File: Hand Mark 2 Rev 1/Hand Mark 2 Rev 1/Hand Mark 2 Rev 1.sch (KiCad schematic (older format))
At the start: 18 parts, among them J1 Conn_ARM_JTAG_SWD_10, M1 Index_Servo, M2 Middle_Servo, M3 Ring_Servo, M4 Pinky_Servo, M5 Thumb_Servo, SW1 Power_Switch

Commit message: changed 3.3 regulator and added resistor to neopixel data input
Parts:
- removed REG1: ADP7142AUJZ-3.3, Package_TO_SOT_SMD:TSOT-23-5, symbol Regulator_Linear:ADP7142AUJZ-3.3
- added C1, C2: 1uF, symbol Device:C
- added R5: 500ohm, symbol Device:R_US
- added REG1: MIC5504-3.3YM5, Package_TO_SOT_SMD:SOT-23-5, symbol Regulator_Linear:MIC5504-3.3YM5
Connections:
- wire segments 38 -> 42
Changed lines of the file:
@@
 EESchema Schematic File Version 4
+LIBS:Hand Mark 2 Rev 1-cache
 EELAYER 30 0
 EELAYER END
@@
 $EndComp
 $Comp
-L Regulator_Linear:ADP7142AUJZ-3.3 REG1
-U 1 1 5E219EEA
-P 1900 1400
-F 0 "REG1" H 1900 1767 50  0000 C CNN
-F 1 "ADP7142AUJZ-3.3" H 1900 1676 50  0000 C CNN
-F 2 "Package_TO_SOT_SMD:TSOT-23-5" H 1900 1000 50  0001 C CIN
-F 3 "https://www.analog.com/media/en/technical-documentation/data-sheets/ADP7142.pdf" H 1900 900 50  0001 C CNN
-	1    1900 1400
-	1    0    0    -1
-$EndComp
-$Comp
 L power:+3.3V #PWR?
 U 1 1 5E22153D
-P 2550 1300
-F 0 "#PWR?" H 2550 1150 50  0001 C CNN
-F 1 "+3.3V" H 2565 1473 50  0000 C CNN
-F 2 "" H 2550 1300 50  0001 C CNN
-F 3 "" H 2550 1300 50  0001 C CNN
-	1    2550 1300
+P 2250 1200
+F 0 "#PWR?" H 2250 1050 50  0001 C CNN
+F 1 "+3.3V" H 2265 1373 50  0000 C CNN
+F 2 "" H 2250 1200 50  0001 C CNN
+F 3 "" H 2250 1200 50  0001 C CNN
+	1    2250 1200
 	1    0    0    -1
 $EndComp
@@
 	1    0    0    -1
 $EndComp
-Wire Wire Line
-	2300 1300 2550 1300
 $Comp
 L power:+3.3V #PWR?
@@
 L power:GND #PWR?
 U 1 1 5E23530E
-P 1900 1700
-F 0 "#PWR?" H 1900 1450 50  0001 C CNN
-F 1 "GND" H 1905 1527 50  0000 C CNN
-F 2 "" H 1900 1700 50  0001 C CNN
-F 3 "" H 1900 1700 50  0001 C CNN
-	1    1900 1700
+P 1700 1800
+F 0 "#PWR?" H 1700 1550 50  0001 C CNN
+F 1 "GND" H 1705 1627 50  0000 C CNN
+F 2 "" H 1700 1800 50  0001 C CNN
+F 3 "" H 1700 1800 50  0001 C CNN
+	1    1700 1800
 	1    0    0    -1
 $EndComp
@@
 L power:+BATT #PWR?
 U 1 1 5E249F42
-P 1300 1300
-F 0 "#PWR?" H 1300 1150 50  0001 C CNN
-F 1 "+BATT" H 1315 1473 50  0000 C CNN
-F 2 "" H 1300 1300 50  0001 C CNN
-F 3 "" H 1300 1300 50  0001 C CNN
-	1    1300 1300
-	1    0    0    -1
-$EndComp
-Wire Wire Line
-	1500 1300 1300 1300
+P 1150 1200
+F 0 "#PWR?" H 1150 1050 50  0001 C CNN
+F 1 "+BATT" H 1165 1373 50  0000 C CNN
+F 2 "" H 1150 1200 50  0001 C CNN
+F 3 "" H 1150 1200 50  0001 C CNN
+	1    1150 1200
+	1    0    0    -1
+$EndComp
 Text GLabel 7600 1350 2    50   Input ~ 0
 MYOSIG
@@
 Wire Wire Line
 	5600 3400 5700 3400
-Text GLabel 7300 4500 0    50   Input ~ 0
+Text GLabel 7100 4500 0    50   Input ~ 0
 NEO
-Wire Wire Line
-	7300 4500 7400 4500
 $Comp
 L power:+5V #PWR?
@@
 	1    0    0    -1
 $EndComp
+$Comp
+L Regulator_Linear:MIC5504-3.3YM5 REG1
+U 1 1 5E20BBC0
+P 1700 1300
+F 0 "REG1" H 1700 1667 50  0000 C CNN
+F 1 "MIC5504-3.3YM5" H 1700 1576 50  0000 C CNN
+F 2 "Package_TO_SOT_SMD:SOT-23-5" H 1700 900 50  0001 C CNN
+F 3 "http://ww1.microchip.com/downloads/en/DeviceDoc/MIC550X.pdf" H 1450 1550 50  0001 C CNN
+	1    1700 1300
+	1    0    0    -1
+$EndComp
+Wire Wire Line
+	2100 1200 2250 1200
+Wire Wire Line
+	1150 1200 1300 1200
+$Comp
+L Device:C C2
+U 1 1 5E21B87C
+P 2250 1650
+F 0 "C2" H 2365 1696 50  0000 L CNN
+F 1 "1uF" H 2365 1605 50  0000 L CNN
+F 2 "" H 2288 1500 50  0001 C CNN
+F 3 "~" H 2250 1650 50  0001 C CNN
+	1    2250 1650
+	1    0    0    -1
+$EndComp
+$Comp
+L Device:C C1
+U 1 1 5E21CD0A
+P 1150 1650
+F 0 "C1" H 1265 1696 50  0000 L CNN
+F 1 "1uF" H 1265 1605 50  0000 L CNN
+F 2 "" H 1188 1500 50  0001 C CNN
+F 3 "~" H 1150 1650 50  0001 C CNN
+	1    1150 1650
+	1    0    0    -1
+$EndComp
+Wire Wire Line
+	2250 1200 2250 1500
+Connection ~ 2250 1200
+Wire Wire Line
+	1150 1200 1150 1500
+Connection ~ 1150 1200
+Wire Wire Line
+	1700 1600 1700 1800
+Wire Wire Line
+	1150 1800 1700 1800
+Connection ~ 1700 1800
+Wire Wire Line
+	1700 1800 2250 1800
+$Comp
+L Device:R_US R5
+U 1 1 5E2292AF
+P 7250 4500
+F 0 "R5" V 7045 4500 50  0000 C CNN
+F 1 "500ohm" V 7136 4500 50  0000 C CNN
+F 2 "" V 7290 4490 50  0001 C CNN
+F 3 "~" H 7250 4500 50  0001 C CNN
+	1    7250 4500
+	0    1    1    0
+$EndComp
 $EndSCHEMATC

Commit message: charger and 5v regulator added. should be ready for breadboard prototyping.
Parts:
- added C? (x2): 4.7uF, symbol Device:C
- added C?: 4.7uF 10V, symbol Device:C
- added C?: 22uF 10V, symbol Device:C
- added L?: 1uH 3A, symbol Device:L
- added LED?: Charging_LED, symbol Device:LED
- added LED?: Charge_Done_LED, symbol Device:LED
- added R?: 2000ohm, symbol Device:R_US
- added R? (x2): 470ohm, symbol Device:R_US
- added R?: 1Mohm, symbol Device:R_US
- added REG?: MIC2876-5.5YMT-TR, symbol hand~parts:MIC2876-5.5YMT-TR
- added USB?: USB_B_Micro, symbol Connector:USB_B_Micro
- renumbered BT1 to BT?, BTN1 to BTN?, C2 to C?, C1 to C?, CHRG1 to CHRG?, J1 to J?, M1 to M?, M2 to M?, M3 to M?, M4 to M?, M5 to M?, MCU1 to MCU?, MYO1 to MYO?, D1 to NEO?, R5 to R?, R1 to R?, R2 to R?, R3 to R?, R4 to R?, REG1 to REG?, SW1 to SW?
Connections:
- wire segments 42 -> 75
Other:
- moved on the sheet: BT?, BTN?, C?, CHRG?, J?, MCU?, NEO?, R?, REG?, SW?

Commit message: starting pcb layout done
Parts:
- BT1: renamed from BT?; footprint (none) -> Connector_JST:JST_EH_S2B-EH_1x02_P2.50mm_Horizontal
- BTN1: renamed from BTN?; footprint (none) -> Connector_JST:JST_EH_S2B-EH_1x02_P2.50mm_Horizontal
- C1, C2, C3, C4, C5, C6: renamed from C?; footprint (none) -> Capacitor_SMD:C_0805_2012Metric_Pad1.15x1.40mm_HandSolder
- J1: renamed from J?; footprint (none) -> Connector_PinHeader_1.27mm:PinHeader_2x05_P1.27mm_Vertical
- L1: renamed from L?; footprint (none) -> Inductor_SMD:L_1210_3225Metric_Pad1.42x2.65mm_HandSolder
- LED1, LED2: renamed from LED?; footprint (none) -> Connector_JST:JST_EH_S2B-EH_1x02_P2.50mm_Horizontal
- M1, M2, M3, M4, M5: renamed from M?; footprint (none) -> Connector_JST:JST_EH_S3B-EH_1x03_P2.50mm_Horizontal
- MYO1: renamed from MYO?; footprint (none) -> Connector_JST:JST_EH_S3B-EH_1x03_P2.50mm_Horizontal
- NEO1: renamed from NEO?; footprint (none) -> Connector_JST:JST_EH_S3B-EH_1x03_P2.50mm_Horizontal
- R1, R2, R3, R4, R5, R6, R7, R8, R9: renamed from R?; footprint (none) -> Resistor_SMD:R_0805_2012Metric_Pad1.15x1.40mm_HandSolder
- REG2: renamed from REG?; footprint (none) -> Package_DFN_QFN:DFN-8-1EP_2x2mm_P0.5mm_EP0.9x1.3mm
- SW1: renamed from SW?; footprint (none) -> Connector_JST:JST_EH_S2B-EH_1x02_P2.50mm_Horizontal
- USB1: renamed from USB?; footprint (none) -> Connector_JST:JST_EH_S2B-EH_1x02_P2.50mm_Horizontal
- gave numbers to parts that had none: 3

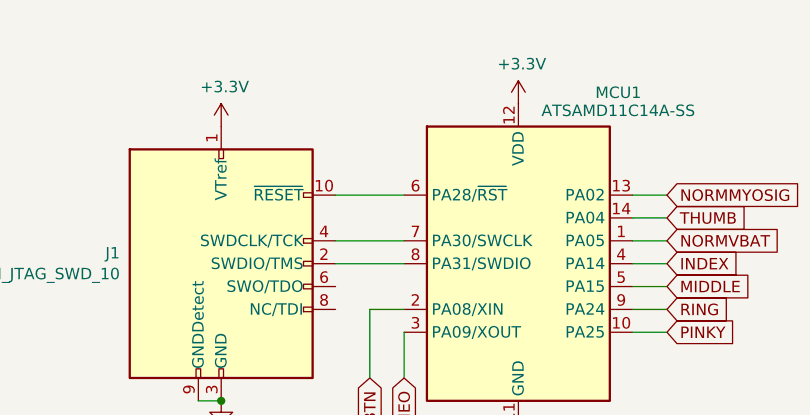
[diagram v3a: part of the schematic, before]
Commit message: finsihed first test routing(need thicker traces for power)
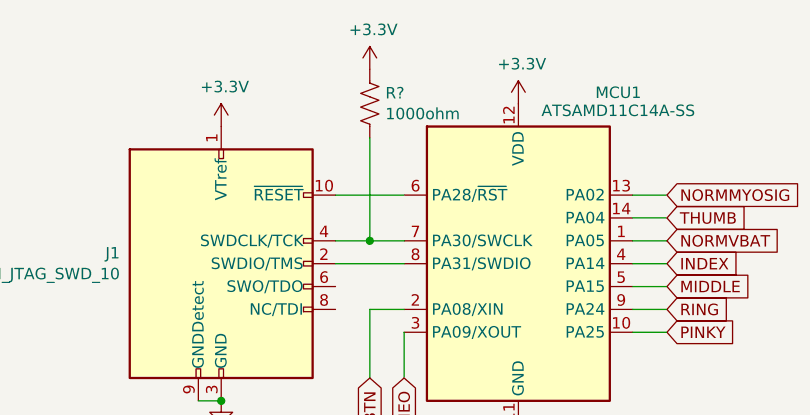
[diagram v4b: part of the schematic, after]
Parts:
- added R?: 1000ohm, symbol Device:R_US
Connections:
- wire segments 75 -> 77
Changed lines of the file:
@@
 	2550 1300 2850 1300
 Wire Wire Line
-	2550 1500 2850 1500
+	2550 1500 2700 1500
 Wire Wire Line
 	2550 1600 2850 1600
@@
 Wire Wire Line
 	4900 5600 5150 5600
+$Comp
+L Device:R_US R?
+U 1 1 5E241226
+P 2700 900
+F 0 "R?" H 2768 946 50  0000 L CNN
+F 1 "1000ohm" H 2768 855 50  0000 L CNN
+F 2 "" V 2740 890 50  0001 C CNN
+F 3 "~" H 2700 900 50  0001 C CNN
+	1    2700 900
+	1    0    0    -1
+$EndComp
+Wire Wire Line
+	2700 1050 2700 1500
+Connection ~ 2700 1500
+Wire Wire Line
+	2700 1500 2850 1500
+$Comp
+L power:+3.3V #PWR?
+U 1 1 5E244CA1
+P 2700 750
+F 0 "#PWR?" H 2700 600 50  0001 C CNN
+F 1 "+3.3V" H 2715 923 50  0000 C CNN
+F 2 "" H 2700 750 50  0001 C CNN
+F 3 "" H 2700 750 50  0001 C CNN
+	1    2700 750
+	1    0    0    -1
+$EndComp
 $EndSCHEMATC

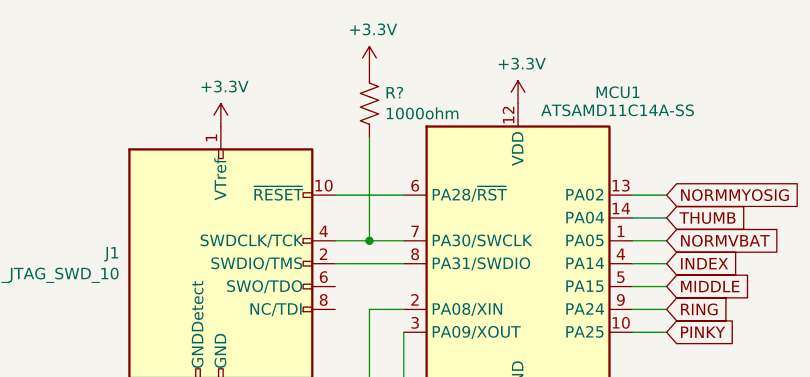
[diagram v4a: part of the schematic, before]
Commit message: added bigger traces to servo power but should be double checked
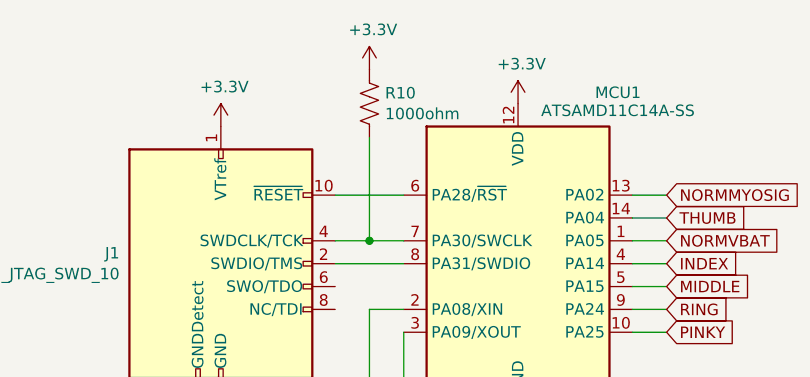
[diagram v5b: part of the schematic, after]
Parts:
- R10: renamed from R?; footprint (none) -> Resistor_SMD:R_0805_2012Metric_Pad1.15x1.40mm_HandSolder
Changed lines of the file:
@@
 	4900 5600 5150 5600
 $Comp
-L Device:R_US R?
+L Device:R_US R10
 U 1 1 5E241226
 P 2700 900
-F 0 "R?" H 2768 946 50  0000 L CNN
+F 0 "R10" H 2768 946 50  0000 L CNN
 F 1 "1000ohm" H 2768 855 50  0000 L CNN
-F 2 "" V 2740 890 50  0001 C CNN
+F 2 "Resistor_SMD:R_0805_2012Metric_Pad1.15x1.40mm_HandSolder" V 2740 890 50  0001 C CNN
 F 3 "~" H 2700 900 50  0001 C CNN
 	1    2700 900
@@
 	2700 1500 2850 1500
 $Comp
-L power:+3.3V #PWR?
+L power:+3.3V #PWR0101
 U 1 1 5E244CA1
 P 2700 750
-F 0 "#PWR?" H 2700 600 50  0001 C CNN
+F 0 "#PWR0101" H 2700 600 50  0001 C CNN
 F 1 "+3.3V" H 2715 923 50  0000 C CNN
 F 2 "" H 2700 750 50  0001 C CNN
